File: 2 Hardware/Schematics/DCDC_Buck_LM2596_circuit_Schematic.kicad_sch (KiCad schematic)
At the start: 7 parts, among them U1 LM2596S-ADJ

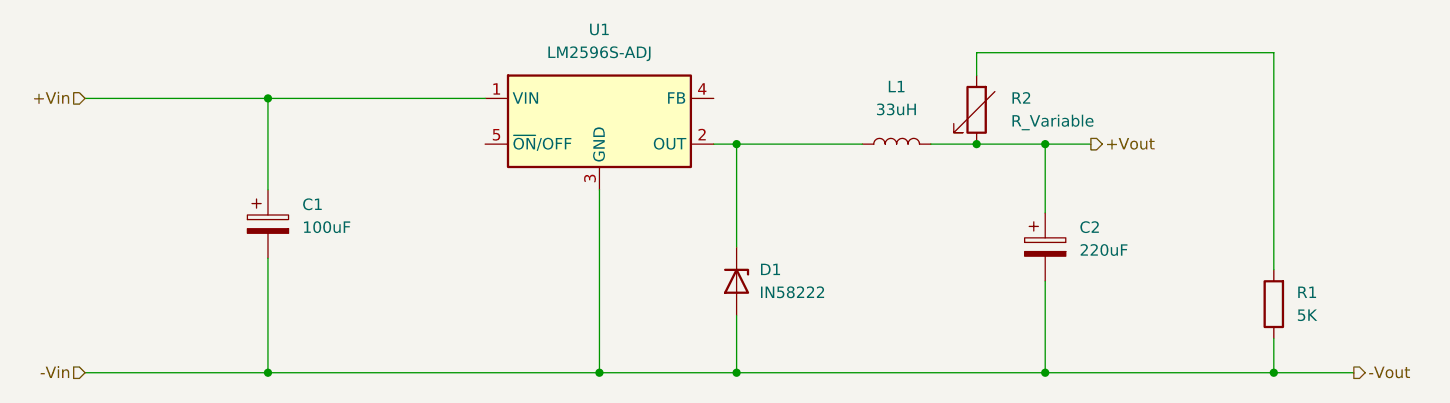
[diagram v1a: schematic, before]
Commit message: Added gitignre, changes (minor) to schematic, changes to horizontal model (WithWheels) and general repo cleanup
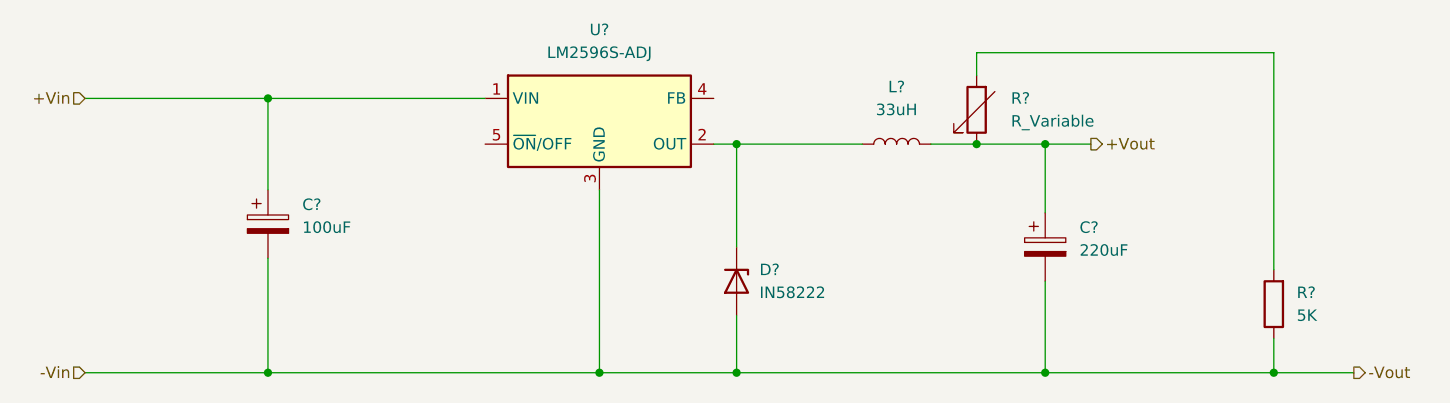
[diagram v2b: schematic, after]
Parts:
- renumbered C1 to C?, C2 to C?, D1 to D?, L1 to L?, R2 to R?, R1 to R?, U1 to U?
